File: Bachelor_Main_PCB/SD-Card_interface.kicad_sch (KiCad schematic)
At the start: 1 part, among them J1 F32Q-1A7H1-11022

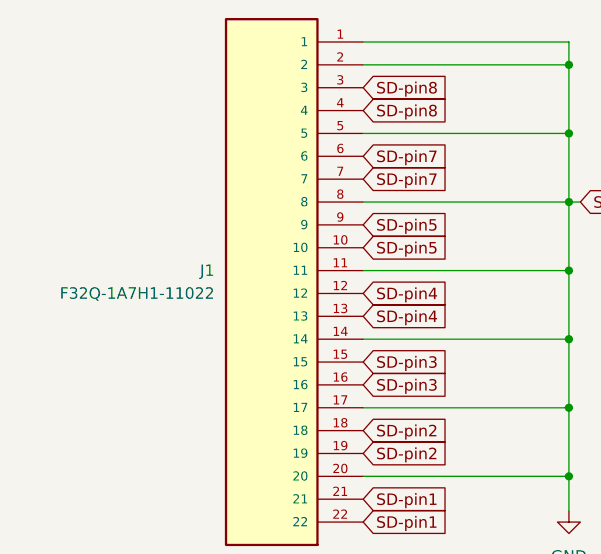
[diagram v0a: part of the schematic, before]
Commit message: Fix anotation of "J" designators and routed ESD suppression on Modem
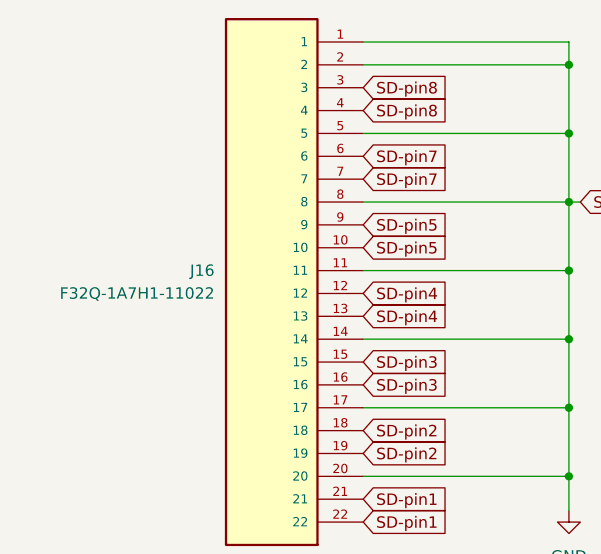
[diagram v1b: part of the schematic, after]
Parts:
- renumbered J1 to J16
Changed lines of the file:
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@@
 		(on_board yes)
 		(dnp no)
-		(property "Reference" "J1"
+		(property "Reference" "J16"
 			(at 97.79 82.5499 0)
 			(effects
@@
 			(project "Bachelor_Main_PCB"
 				(path "/3544d663-329e-4884-b753-28436ca187e8/e2053849-b1b4-4732-a0d8-f90e27301853"
-					(reference "J1")
+					(reference "J16")
 					(unit 1)
 				)

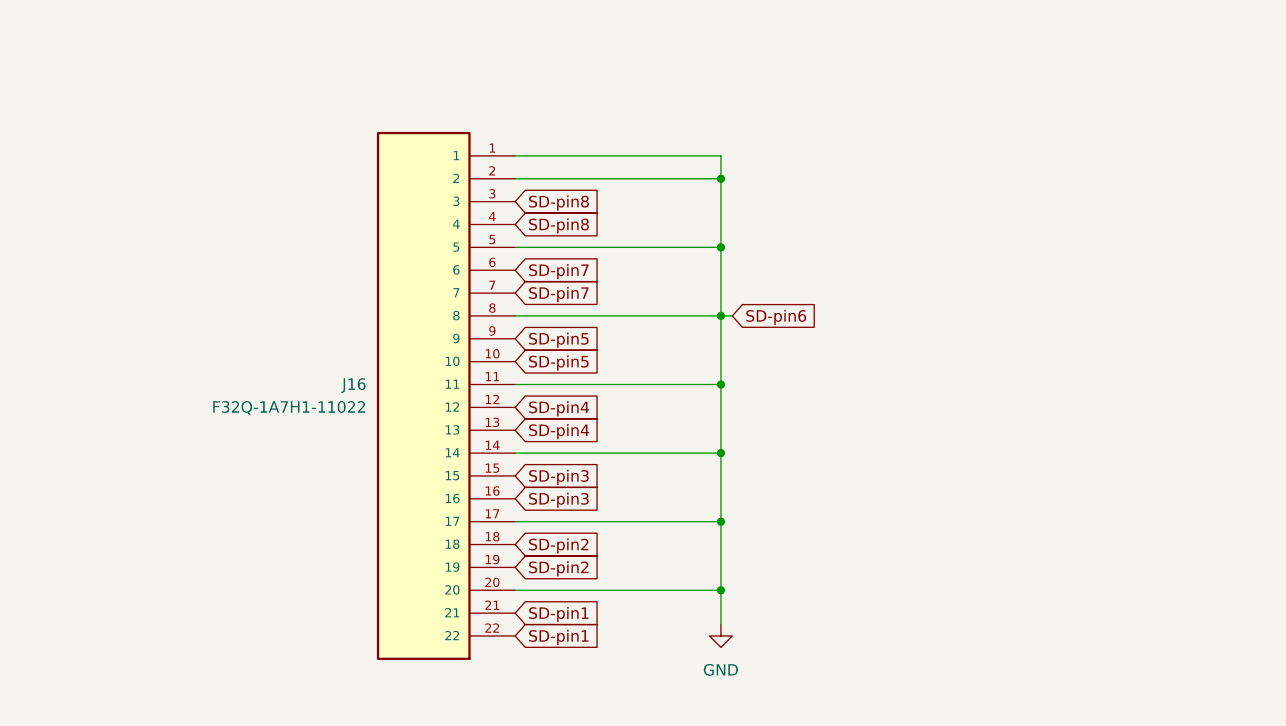
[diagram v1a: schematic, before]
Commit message: Add SD CARD pullups
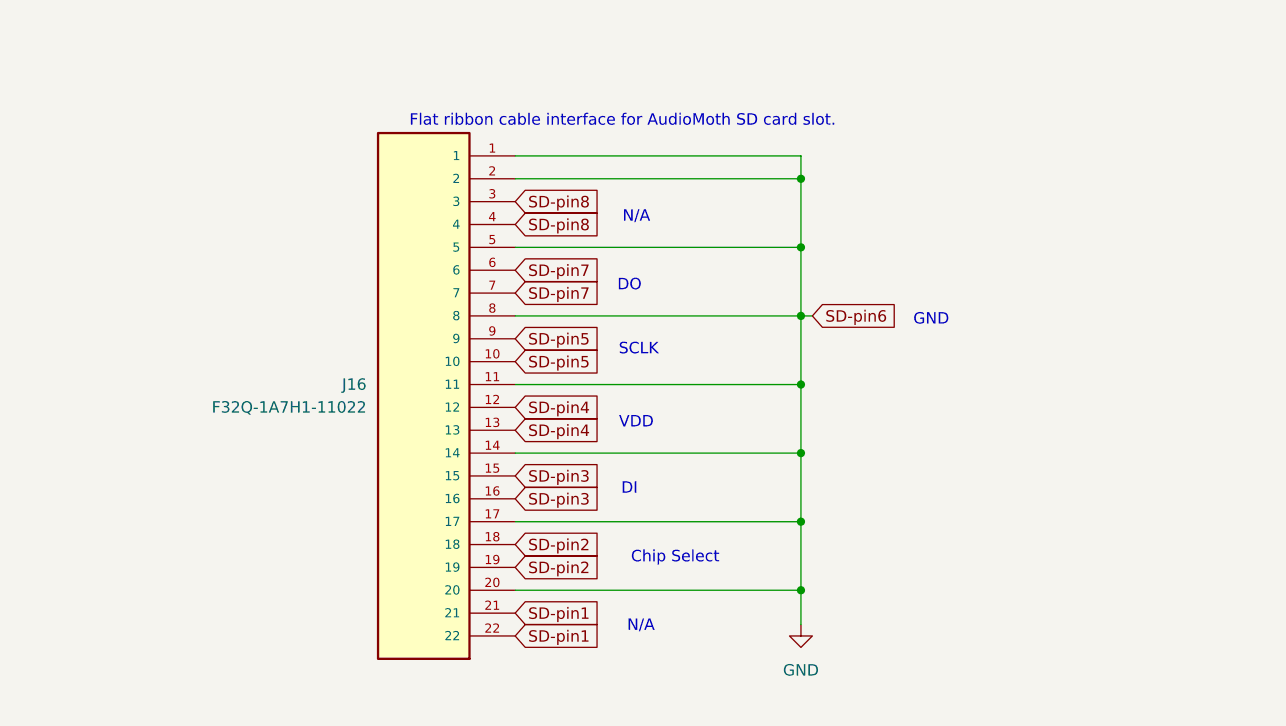
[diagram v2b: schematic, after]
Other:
- note added: "Chip Select"
- note added: "DI"
- note added: "DO"
- note added: "Flat ribbon cable interface for AudioMoth SD card slot."
- note added: "GND"
- note added: "N/A"
- note added: "SCLK"
- note added: "VDD"

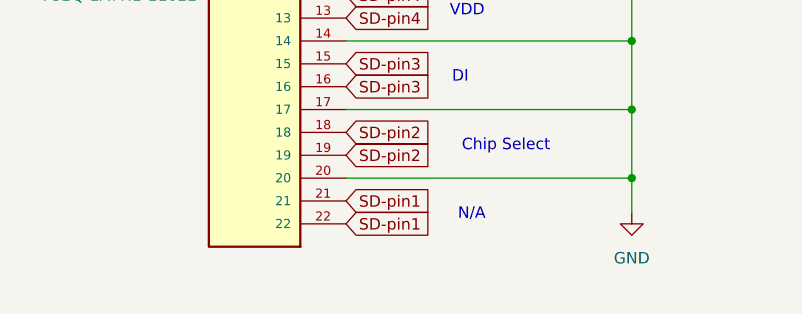
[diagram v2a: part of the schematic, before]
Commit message: Added text to SD audiomoth interface
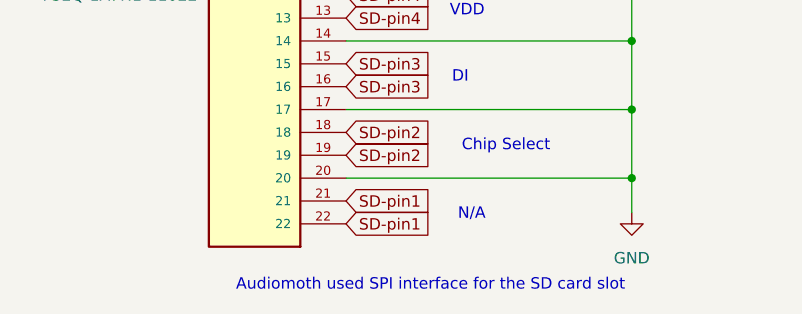
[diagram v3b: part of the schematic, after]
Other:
- note added: "Audiomoth used SPI interface for the SD card slot"
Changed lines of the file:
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@@
+		)
+	)
+	(text "Audiomoth used SPI interface for the SD card slot"
+		(exclude_from_sim no)
+		(at 123.698 117.348 0)
+		(effects
+			(font
+				(size 1.27 1.27)
+			)
 		)
 	)

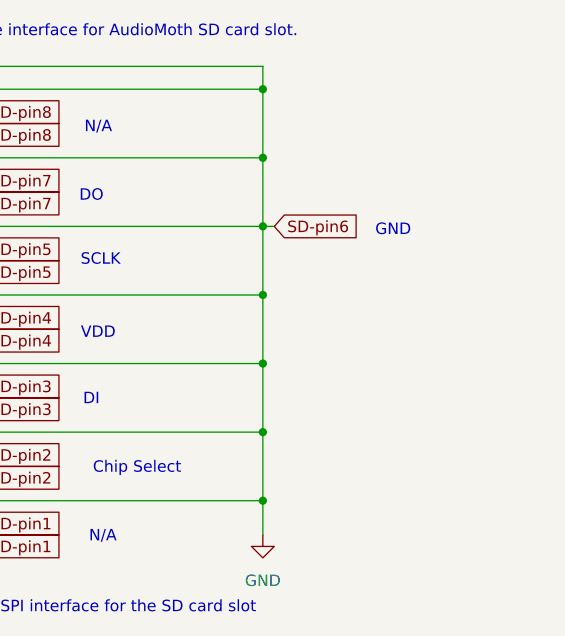
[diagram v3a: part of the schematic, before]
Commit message: Add audiomoth to MCU SPI
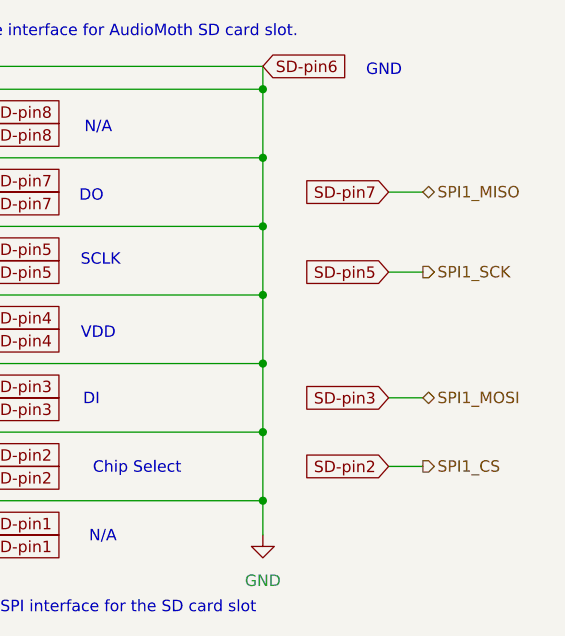
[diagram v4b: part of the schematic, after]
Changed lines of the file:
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@@
 	(text "GND"
 		(exclude_from_sim no)
-		(at 160.528 75.438 0)
+		(at 159.512 57.658 0)
 		(effects
 			(font
@@
 	(wire
 		(pts
-			(xy 147.32 74.93) (xy 146.05 74.93)
+			(xy 160.02 80.01) (xy 163.83 80.01)
 		)
 		(stroke
@@
 	(wire
 		(pts
+			(xy 163.83 101.6) (xy 160.02 101.6)
+		)
+		(stroke
+			(width 0)
+			(type default)
+		)
+	)
+	(wire
+		(pts
 			(xy 146.05 74.93) (xy 146.05 67.31)
 		)
@@
 	(wire
 		(pts
+			(xy 160.02 71.12) (xy 163.83 71.12)
+		)
+		(stroke
+			(width 0)
+			(type default)
+		)
+	)
+	(wire
+		(pts
 			(xy 114.3 67.31) (xy 146.05 67.31)
 		)
@@
 	(wire
 		(pts
+			(xy 160.02 93.98) (xy 163.83 93.98)
+		)
+		(stroke
+			(width 0)
+			(type default)
+		)
+	)
+	(wire
+		(pts
 			(xy 146.05 74.93) (xy 146.05 82.55)
 		)
@@
 		)
 	)
+	(global_label "SD-pin7"
+		(shape input)
+		(at 160.02 71.12 180)
+		(fields_autoplaced yes)
+		(effects
+			(font
+				(size 1.27 1.27)
+			)
+			(justify right)
+		)
+		(property "Intersheetrefs" "${INTERSHEET_REFS}"
+			(at 148.8706 71.12 0)
+			(effects
+				(font
+					(size 1.27 1.27)
+				)
+				(justify right)
+				(hide yes)
+			)
+		)
+	)
 	(global_label "SD-pin8"
 		(shape input)
@@
 		)
 	)
+	(global_label "SD-pin2"
+		(shape input)
+		(at 160.02 101.6 180)
+		(fields_autoplaced yes)
+		(effects
+			(font
+				(size 1.27 1.27)
+			)
+			(justify right)
+		)
+		(property "Intersheetrefs" "${INTERSHEET_REFS}"
+			(at 148.8706 101.6 0)
+			(effects
+				(font
+					(size 1.27 1.27)
+				)
+				(justify right)
+				(hide yes)
+			)
+		)
+	)
 	(global_label "SD-pin3"
 		(shape input)
@@
 		)
 	)
+	(global_label "SD-pin3"
+		(shape input)
+		(at 160.02 93.98 180)
+		(fields_autoplaced yes)
+		(effects
+			(font
+				(size 1.27 1.27)
+			)
+			(justify right)
+		)
+		(property "Intersheetrefs" "${INTERSHEET_REFS}"
+			(at 148.8706 93.98 0)
+			(effects
+				(font
+					(size 1.27 1.27)
+				)
+				(justify right)
+				(hide yes)
+			)
+		)
+	)
 	(global_label "SD-pin6"
 		(shape input)
-		(at 147.32 74.93 0)
-		(fields_autoplaced yes)
-		(effects
-			(font
-				(size 1.27 1.27)
-			)
-			(justify left)
-		)
-		(property "Intersheetrefs" "${INTERSHEET_REFS}"
-			(at 158.4694 74.93 0)
-			(effects
-				(font
-					(size 1.27 1.27)
-				)
-				(justify left)
+		(at 146.05 57.15 0)
+		(fields_autoplaced yes)
+		(effects
+			(font
+				(size 1.27 1.27)
+			)
+			(justify left)
+		)
+		(property "Intersheetrefs" "${INTERSHEET_REFS}"
+			(at 157.1994 57.15 0)
+			(effects
+				(font
+					(size 1.27 1.27)
+				)
+				(justify left)
+				(hide yes)
+			)
+		)
+	)
+	(global_label "SD-pin5"
+		(shape input)
+		(at 160.02 80.01 180)
+		(fields_autoplaced yes)
+		(effects
+			(font
+				(size 1.27 1.27)
+			)
+			(justify right)
+		)
+		(property "Intersheetrefs" "${INTERSHEET_REFS}"
+			(at 148.8706 80.01 0)
+			(effects
+				(font
+					(size 1.27 1.27)
+				)
+				(justify right)
 				(hide yes)
 			)
@@
 		)
 	)
+	(hierarchical_label "SPI1_MOSI"
+		(shape bidirectional)
+		(at 163.83 93.98 0)
+		(effects
+			(font
+				(size 1.27 1.27)
+			)
+			(justify left)
+		)
+	)
+	(hierarchical_label "SPI1_SCK"
+		(shape output)
+		(at 163.83 80.01 0)
+		(effects
+			(font
+				(size 1.27 1.27)
+			)
+			(justify left)
+		)
+	)
+	(hierarchical_label "SPI1_CS"
+		(shape output)
+		(at 163.83 101.6 0)
+		(effects
+			(font
+				(size 1.27 1.27)
+			)
+			(justify left)
+		)
+	)
+	(hierarchical_label "SPI1_MISO"
+		(shape bidirectional)
+		(at 163.83 71.12 0)
+		(effects
+			(font
+				(size 1.27 1.27)
+			)
+			(justify left)
+		)
+	)

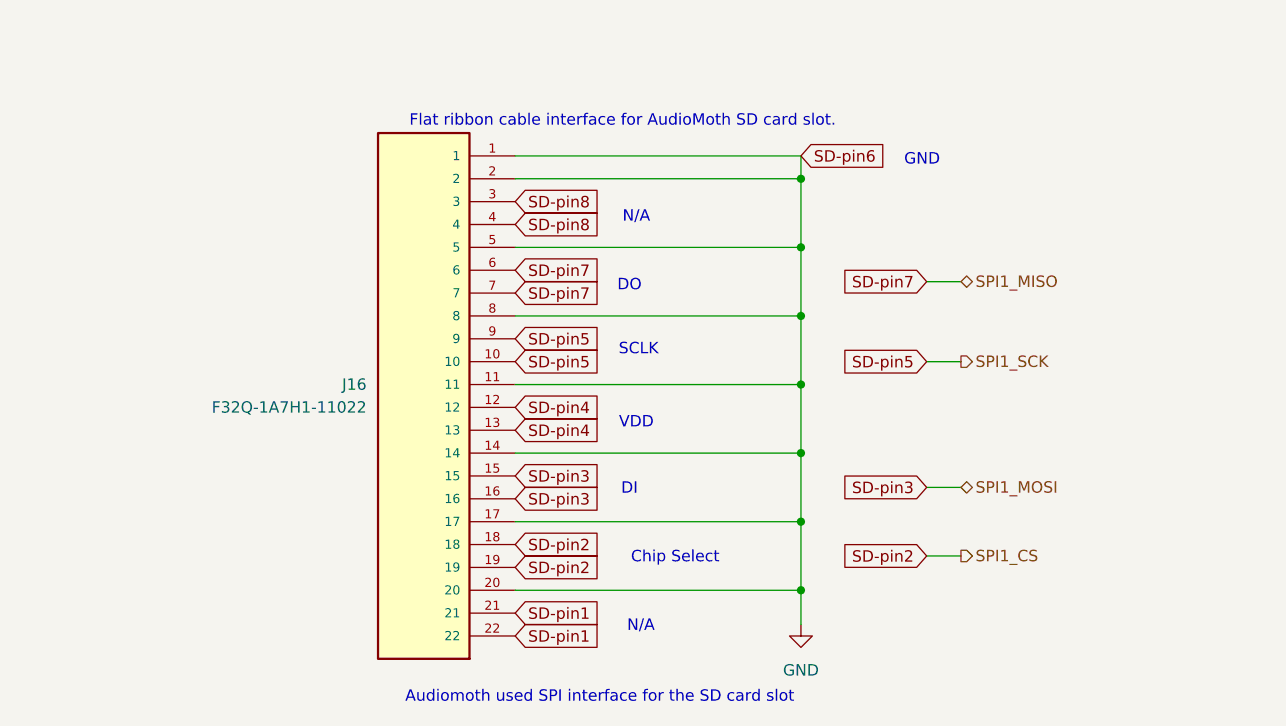
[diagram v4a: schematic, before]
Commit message: Add Vin sampling and route V_IN and V_IMON to MCU sheet
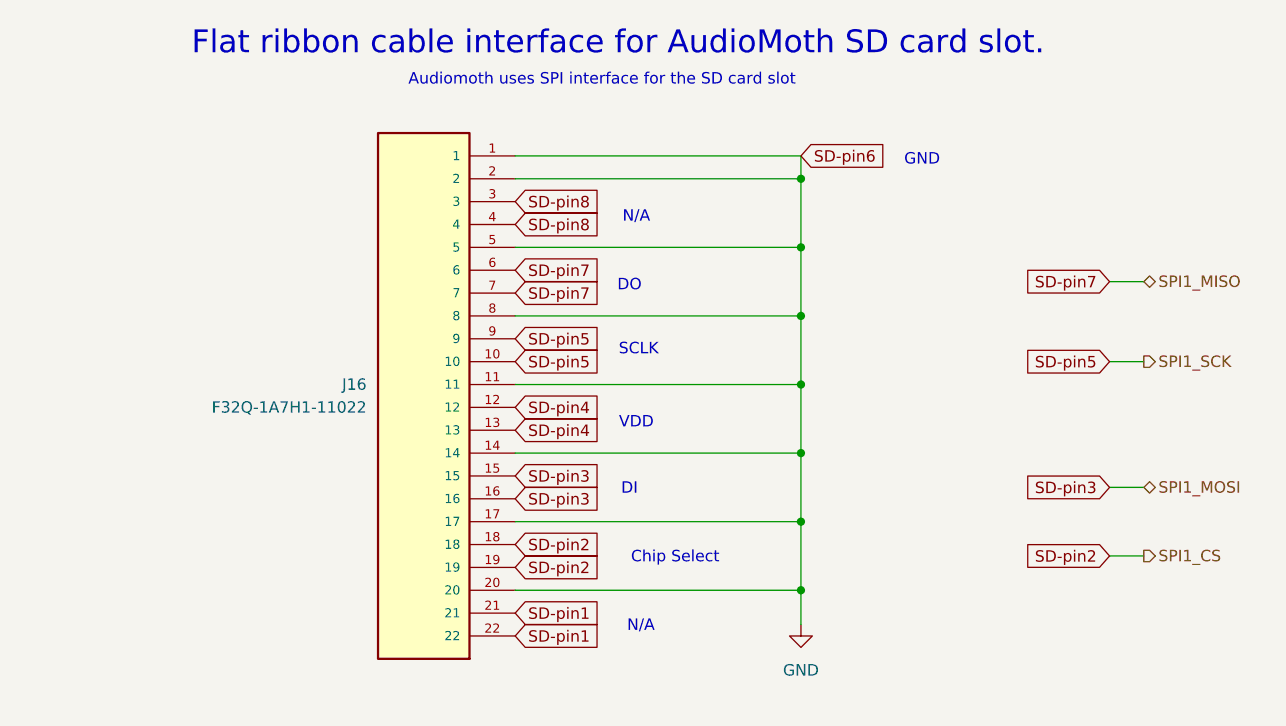
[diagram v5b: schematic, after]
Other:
- note added: "Audiomoth uses SPI interface for the SD card slot"
- note removed: "Audiomoth used SPI interface for the SD card slot"
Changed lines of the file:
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@@
 	(text "Flat ribbon cable interface for AudioMoth SD card slot."
 		(exclude_from_sim no)
-		(at 126.238 53.34 0)
-		(effects
-			(font
-				(size 1.27 1.27)
+		(at 125.73 44.704 0)
+		(effects
+			(font
+				(size 2.54 2.54)
 			)
 		)
@@
 		)
 	)
-	(text "Audiomoth used SPI interface for the SD card slot"
-		(exclude_from_sim no)
-		(at 123.698 117.348 0)
+	(text "Audiomoth uses SPI interface for the SD card slot"
+		(exclude_from_sim no)
+		(at 123.952 48.768 0)
 		(effects
 			(font
@@
 	(wire
 		(pts
-			(xy 160.02 80.01) (xy 163.83 80.01)
+			(xy 180.34 80.01) (xy 184.15 80.01)
 		)
 		(stroke
@@
 	(wire
 		(pts
-			(xy 163.83 101.6) (xy 160.02 101.6)
+			(xy 184.15 101.6) (xy 180.34 101.6)
 		)
 		(stroke
@@
 	(wire
 		(pts
-			(xy 160.02 71.12) (xy 163.83 71.12)
+			(xy 180.34 71.12) (xy 184.15 71.12)
 		)
 		(stroke
@@
 	(wire
 		(pts
-			(xy 160.02 93.98) (xy 163.83 93.98)
+			(xy 180.34 93.98) (xy 184.15 93.98)
 		)
 		(stroke
@@
 	(global_label "SD-pin7"
 		(shape input)
-		(at 160.02 71.12 180)
+		(at 180.34 71.12 180)
 		(fields_autoplaced yes)
 		(effects
@@
 		)
 		(property "Intersheetrefs" "${INTERSHEET_REFS}"
-			(at 148.8706 71.12 0)
+			(at 169.1906 71.12 0)
 			(effects
 				(font
@@
 	(global_label "SD-pin2"
 		(shape input)
-		(at 160.02 101.6 180)
+		(at 180.34 101.6 180)
 		(fields_autoplaced yes)
 		(effects
@@
 		)
 		(property "Intersheetrefs" "${INTERSHEET_REFS}"
-			(at 148.8706 101.6 0)
+			(at 169.1906 101.6 0)
 			(effects
 				(font
@@
 	(global_label "SD-pin3"
 		(shape input)
-		(at 160.02 93.98 180)
+		(at 180.34 93.98 180)
 		(fields_autoplaced yes)
 		(effects
@@
 		)
 		(property "Intersheetrefs" "${INTERSHEET_REFS}"
-			(at 148.8706 93.98 0)
+			(at 169.1906 93.98 0)
 			(effects
 				(font
@@
 	(global_label "SD-pin5"
 		(shape input)
-		(at 160.02 80.01 180)
+		(at 180.34 80.01 180)
 		(fields_autoplaced yes)
 		(effects
@@
 		)
 		(property "Intersheetrefs" "${INTERSHEET_REFS}"
-			(at 148.8706 80.01 0)
+			(at 169.1906 80.01 0)
 			(effects
 				(font
@@
 	(hierarchical_label "SPI1_MOSI"
 		(shape bidirectional)
-		(at 163.83 93.98 0)
+		(at 184.15 93.98 0)
 		(effects
 			(font
@@
 	(hierarchical_label "SPI1_SCK"
 		(shape output)
-		(at 163.83 80.01 0)
+		(at 184.15 80.01 0)
 		(effects
 			(font
@@
 	(hierarchical_label "SPI1_CS"
 		(shape output)
-		(at 163.83 101.6 0)
+		(at 184.15 101.6 0)
 		(effects
 			(font
@@
 	(hierarchical_label "SPI1_MISO"
 		(shape bidirectional)
-		(at 163.83 71.12 0)
-		(effects
-			(font
+		(at 184.15 71.12 0)
+		(effects
+			(font
